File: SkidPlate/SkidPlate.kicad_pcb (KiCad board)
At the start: 2 copper layers, 152.1 x 80.1 mm, 164 parts, among them J2 USB4145-03-0170-C, J3 JST_BM04B-GHS-TBT, J4 JST_2P_LIMITSW, J5 Conn_02x09_Counter_Clockwise, Q2 IRFR3410TRPBF_alternate, Q3 FGH50T65SQD-F155, Q7 FGH50T65SQD-F155, T1 DA2034, U1 RPI2040, U10 SW_TS-1187A-B-A-B, U11 AMP_MCP6231UT_alternate, U2 BNO055, U2 MCP14A0454-E/SN_alternate, U3 AMS1117-3.3, U3 IC_PMW3360DM-T2QU, U4 LT3750, U6 SN65HVD233, U7 MCP2515-xST, U8 AMP_MCP6231UT_alternate, U9 SW_TS-1187A-B-A-B, Y1 XTAL-12MHZ-YXC, Y2 ABM3-8.000MHZ-D2Y-T(alternate)

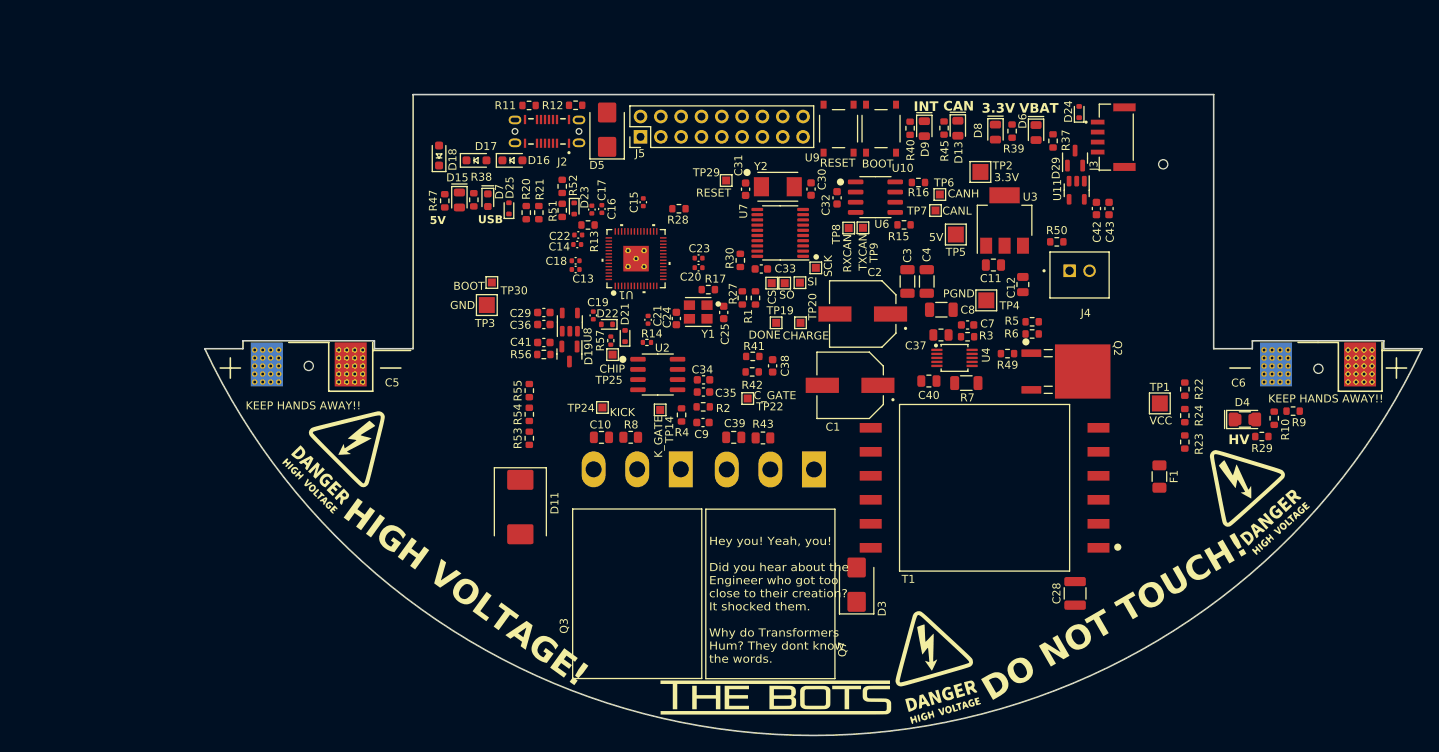
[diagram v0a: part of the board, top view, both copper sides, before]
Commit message: updated skidplate schematic, need to add usb pd
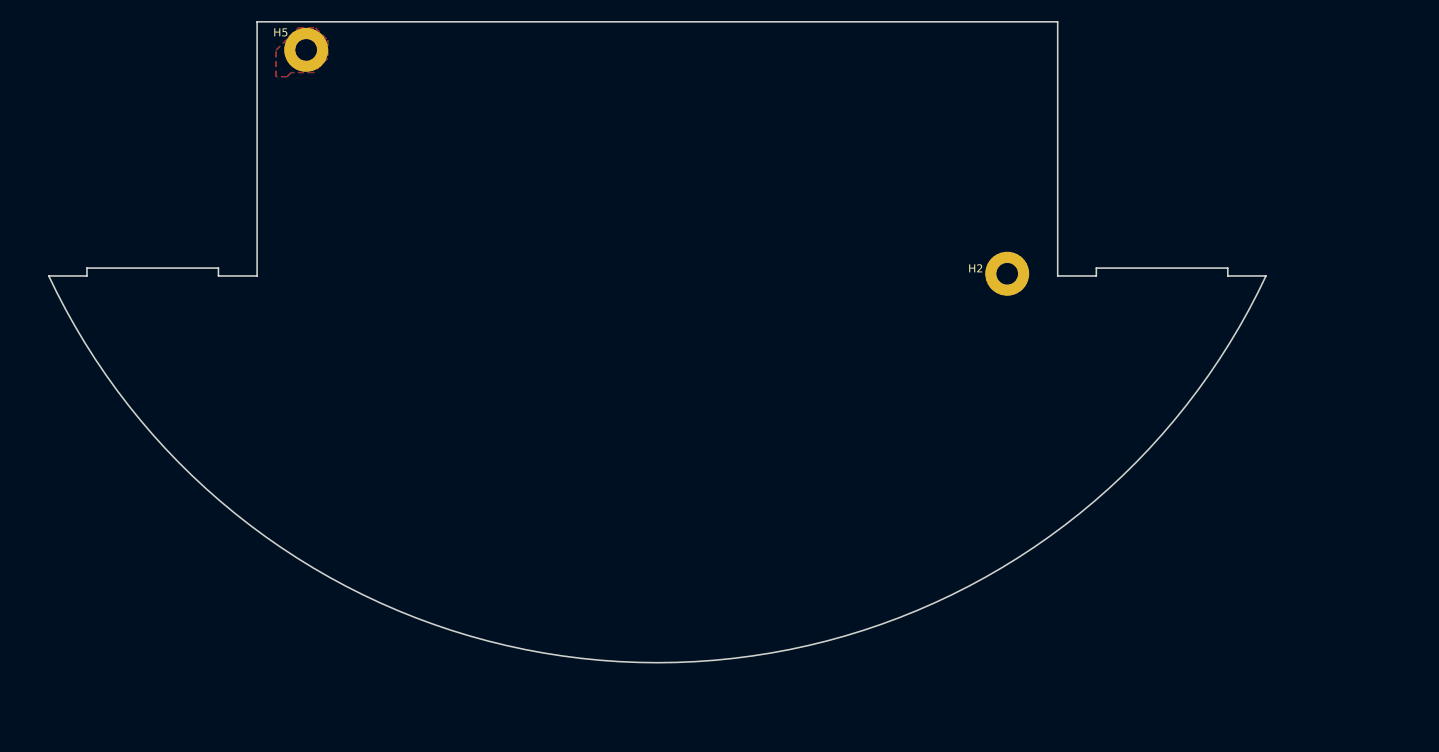
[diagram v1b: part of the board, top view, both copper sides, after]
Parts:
- removed the C1 at (170.6, 106.3)
- removed C10, C39: 1500p, bots:C_0805_2012Metric
- removed C11, C12, C37, C40: 10u, bots:C_0805_2012Metric
- removed C13, C14, C15, C16, C18, C19, C20, C21: 0.1u_0402, bots:C_0402_1005Metric
- removed C17, C22, C23: 1u_0402, bots:C_0402_1005Metric
- removed the C2 at (172.2, 97.4)
- removed C24, C25: 27p, bots:C_0603_1608Metric
- removed C28: 0.1u_600V, bots:C_1210_3225Metric
- removed C29, C41, C43: 0.01u, bots:C_0603_1608Metric
- removed the C3 at (177.8, 93.4)
- removed C30, C31: 22p, bots:C_0603_1608Metric
- removed C32, C33, C34, C38, C9: 0.1u, bots:C_0603_1608Metric
- removed C35, C36, C42: 1u, bots:C_0603_1608Metric
- removed the C4 at (180.2, 93.4)
- removed C5: 1000u, bots:CP_Radial_Horizontal_D25.4mm_H45mm
- removed C6: 1000u, bots:CP_Radial_Horizontal_D25.4mm_H45mm_reversed
- removed C7: 100p, bots:C_0603_1608Metric
- removed C8: 22u_1206, bots:C_1206_3216Metric
- removed D11: MUR860J_alternate, bots:D_SMC
- removed D13, D15, D6, D8, D9: LED, bots:LED_0805_2012Metric
- removed D16, D17, D18: 220mV Schottky, bots:D_SOD-323_HandSoldering
- removed D19, D29: H3V3HT2U, bots:SOT-23
- removed D21, D22, D23, D24, D25: BZT52C3V3T-7, bots:D_SOD-523
- removed D3: MURS160-E3/52T_alternate, bots:D_SMB
- removed D4: LED_red, bots:LED_1206MERGE0805
- removed D5: SMBJ5338B-TP_alternate, bots:D_SMB
- removed D7: LED_blue, bots:LED_0603_1608Metric
- removed F1: 0501010.WR1, bots:Fuse_1206_3216Metric
- removed G*** (x2): SILK_Danger, bots:SILK_Danger
- removed G***: SILK_TheBotsLogo, bots:SILK_TheBotsLogo
- removed G***: LOGO, LOGO
- removed H10, H11, H12: ToolingHoleJLC, bots:ToolingHoleJLC
- removed J2: USB4145-03-0170-C, bots:GCT_USB4145-03-0170-C_REVA2
- removed J3: JST_BM04B-GHS-TBT, bots:JST_BM04B-GHS-TBT
- removed J4: JST_2P_LIMITSW, bots:JST_B2B-XH-A_LF__SN_
- removed J5: Conn_02x09_Counter_Clockwise, bots:PinHeader_2x09_P2.54mm_Vertical
- removed Q2: IRFR3410TRPBF_alternate, bots:DPAK-3_ONS
- removed Q3, Q7: FGH50T65SQD-F155, bots:TO-247-3_Horizontal_TabDown
- removed R1, R10, R27, R29, R50, R9: 100k, bots:R_0603_1608Metric
- removed R11, R12: 5.1k, bots:R_0603_1608Metric
- removed R13: 200R, bots:R_0603_1608Metric
- removed R14, R57: 0R, bots:R_0402_1005Metric
- removed R15, R16, R2, R28, R30, R41: 10k, bots:R_0603_1608Metric
- removed R17, R39: 1k, bots:R_0603_1608Metric
- removed R20, R21: 33R, bots:R_0603_1608Metric
- removed R22: R_200k, bots:R_0603_1608Metric
- removed R23, R24: R_470k, bots:R_0603_1608Metric
- removed R3: 2.4k, bots:R_0603_1608Metric
- removed R37: 47k, bots:R_0603_1608Metric
- removed R38: 820R, bots:R_0603_1608Metric
- removed R4, R42: 75R, bots:R_0603_1608Metric
- removed R40, R45: 510R, bots:R_0603_1608Metric
- removed R43, R8: 2, bots:R_0805_2012Metric
- removed R47: 2k, bots:R_0603_1608Metric
- removed R49: R_0OHM_JUMPER, bots:R_0603_1608Metric
- removed R5: 40.2k, bots:R_0603_1608Metric
- removed R51: 51k, bots:R_0603_1608Metric
- removed R52: 30k, bots:R_0603_1608Metric
- removed R53, R54, R55: 330k, bots:R_0603_1608Metric
- removed R56: 13k, bots:R_0603_1608Metric
- removed R6: 33k, bots:R_0603_1608Metric
- removed R7: 8m, bots:R_1206_3216Metric
- removed T1: DA2034, bots:DA2034-ALD_COC
- removed TP1: VCC, bots:TestPoint_Pad_2.0x2.0mm
- removed TP10: SI, bots:TestPoint_Pad_1.0x1.0mm
- removed TP11: SO, bots:TestPoint_Pad_1.0x1.0mm
- removed TP12: CS, bots:TestPoint_Pad_1.0x1.0mm
- removed TP13: SCK, bots:TestPoint_Pad_1.0x1.0mm
- removed TP14: K_GATE, bots:TestPoint_Pad_1.0x1.0mm
- removed TP19: DONE, bots:TestPoint_Pad_1.0x1.0mm
- removed TP2: 3.3V, bots:TestPoint_Pad_2.0x2.0mm
- removed TP20: CHARGE, bots:TestPoint_Pad_1.0x1.0mm
- removed TP22: C_GATE, bots:TestPoint_Pad_1.0x1.0mm
- removed TP24: KICK, bots:TestPoint_Pad_1.0x1.0mm
- removed TP25: CHIP, bots:TestPoint_Pad_1.0x1.0mm
- removed TP29: RESET, bots:TestPoint_Pad_1.0x1.0mm
- removed TP3: GND, bots:TestPoint_Pad_2.0x2.0mm
- removed TP30: BOOT, bots:TestPoint_Pad_1.0x1.0mm
- removed TP4: PGND, bots:TestPoint_Pad_2.0x2.0mm
- removed TP5: 5V, bots:TestPoint_Pad_2.0x2.0mm
- removed TP6: CANH, bots:TestPoint_Pad_1.0x1.0mm
- removed TP7: CANL, bots:TestPoint_Pad_1.0x1.0mm
- removed TP8: RXCAN, bots:TestPoint_Pad_1.0x1.0mm
- removed TP9: TXCAN, bots:TestPoint_Pad_1.0x1.0mm
- removed the U1 at (143.9, 90.5)
- removed U10, U9: SW_TS-1187A-B-A-B, bots:SW_TS-1187A-B-A-B
- removed U11, U8: AMP_MCP6231UT_alternate, bots:SOT-23-5
- removed the U2 at (146.6, 105.0)
- removed the U3 at (189.9, 85.7)
- removed the U4 at (183.7, 102.9)
- removed U6: SN65HVD233, bots:SOIC-8_3.9x4.9mm_P1.27mm
- removed U7: MCP2515-xST, bots:TSSOP-20_4.4x6.5mm_P0.65mm
- removed Y1: XTAL-12MHZ-YXC, bots:SMD3225-4P
- removed Y2: ABM3-8.000MHZ-D2Y-T(alternate), bots:ABM3
- added H2: PGND, bots:MountingHole_2.7mm_M2.5_DIN965_Pad, F.Cu at (190.3, 92.4)
- added H5: 5V, bots:MountingHole_2.7mm_M2.5_DIN965_Pad, F.Cu at (102.6, 64.4)
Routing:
- added copper zone on F.Cu, net /PowerPillars/5V_IN
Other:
- board text removed: "3.3V"
- board text removed: "5V"
- board text removed: "BOOT"
- board text removed: "CAN"
- board text removed: "DO NOT TOUCH!"
- board text removed: "HIGH VOLTAGE!"
- board text removed: "HV"
- board text removed: "Hey you! Yeah, you! Did you hear about the Engineer who got too close to their creation? It shocked them. Why do Transformers Hum? They dont know the words."
- board text removed: "INT"
- board text removed: "KEEP HANDS AWAY!!"
- board text removed: "RESET"
- board text removed: "USB"
- board text removed: "VBAT"

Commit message: midplate additions WIP
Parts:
- removed C1: 100n, bots:C_0603_1608Metric
- removed C2: 100nF, Capacitor_SMD:C_1206_3216Metric
- removed the H2 at (190.3, 92.4)
- removed the H2 at (-17.7, 86.0)
- removed U3: IC_PMW3360DM-T2QU, bots:IC_PMW3360DM-T2QU 16Pin
- removed U4: ~, Package_TO_SOT_SMD:SOT-223
- added H2: PGND, bots:MountingHole_2.7mm_M2.5_DIN965_Pad, F.Cu at (195.4, 120.4)
- added H3: CANL, bots:MountingHole_2.7mm_M2.5_DIN965_Pad, F.Cu at (195.4, 102.8)
- added H4: CANH, bots:MountingHole_2.7mm_M2.5_DIN965_Pad, F.Cu at (195.4, 92.4)
- added H6: EXTRA, bots:MountingHole_2.7mm_M2.5_DIN965_Pad, F.Cu at (107.7, 124.7)
- added H7: HV, bots:MountingHole_2.7mm_M2.5_DIN965_Pad, F.Cu at (107.7, 133.4)
- added H8: CHICKER, bots:MountingHole_2.7mm_M2.5_DIN965_Pad, F.Cu at (107.7, 142.2)
- added H9: BKBM, bots:MountingHole_2.7mm_M2.5_DIN965_Pad, F.Cu at (107.7, 107.6)
- added J11: XT30UPB-M, bots:AMASS_XT30UPB-M, F.Cu at (41.2, 37.2)
- added J12: XT30UPB-M, bots:AMASS_XT30UPB-M, F.Cu at (41.2, 43.9)
- added J13: XT30UPB-M, bots:AMASS_XT30UPB-M, F.Cu at (41.2, 50.7)
- added J14: XT30UPB-M, bots:AMASS_XT30UPB-M, F.Cu at (41.2, 57.4)
- added J3: JST_BM03B-GHS-TBT, bots:JST_BM03B-GHS-TBT, F.Cu at (56.7, 64.5)
- added J4: JST_BM04B-GHS-TBT, bots:JST_BM04B-GHS-TBT, F.Cu at (57.3, 33.8)
- added J5: JST_BM04B-GHS-TBT, bots:JST_BM04B-GHS-TBT, F.Cu at (57.3, 41.5)
- added J6: JST_BM04B-GHS-TBT, bots:JST_BM04B-GHS-TBT, F.Cu at (57.3, 49.2)
- added J7: JST_BM04B-GHS-TBT, bots:JST_BM04B-GHS-TBT, F.Cu at (57.3, 56.9)
- added R2: 20k, Resistor_SMD:R_0603_1608Metric, F.Cu at (54.3, 68.0)
- added R3: 10k, Resistor_SMD:R_0603_1608Metric, F.Cu at (54.3, 70.5)
- added TP1: SI, bots:pad_0603, F.Cu at (29.4, 70.0)
- added TP11: VCC, bots:TestPoint_Pad_2.0x2.0mm, F.Cu at (29.8, 82.7)
- added TP2: SI, bots:pad_0603, F.Cu at (29.4, 72.4)
- added TP3: SI, bots:pad_0603, F.Cu at (29.4, 74.7)
- added TP4: SI, bots:pad_0603, F.Cu at (29.4, 77.1)
- added TP5: SI, bots:pad_0603, F.Cu at (29.4, 79.5)
- C3: value 10uF -> 10u; footprint Capacitor_SMD:C_1206_3216Metric -> bots:C_0805_2012Metric
- C4: value 10uF -> 22u; footprint bots:CAP_25SVPF100M -> bots:C_0603_1608Metric
- H1: value 5V -> VCC
- U1: value ~ -> AMS1117-3.3; footprint bots:RV1106_PICO_MAX -> bots:SOT-223-3_TabPin2
- U2: value BNO055 -> LSM6DSOX; footprint bots:LGA28R50P4X10_380X520X100 -> bots:PQFN50P300X250X86-14N
- moved H1 222.2 mm to (195.4, 142.2)
- moved U1 69.6 mm to (37.3, 102.4)
- moved U2 54.0 mm to (46.1, 96.8)
- moved C3 49.2 mm to (30.9, 104.8), turned to 180 degrees
- moved C4 44.8 mm to (31.9, 101.2), turned to 90 degrees
- moved H5 28.5 mm to (107.7, 92.4)
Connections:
- H1 pad 1: +5V -> VCC
- H5 pad 1: /PowerPillars/5V_IN -> +5V
- U1 pad 1: unconnected-(U1-GPIO1_B3_d-Pad1) -> GND
- U1 pad 2: unconnected-(U1-GPIO1_B3_u-Pad2) -> +3V3
- U1 pad 3: GND -> +5V
- U2 pad 1: (no net) -> unconnected-(U2-SDO/SA0-Pad1)
- U2 pad 10: /GNDIO -> unconnected-(U2-OCS_AUX-Pad10)
- U2 pad 11: IMU_RST -> unconnected-(U2-SDO_AUX-Pad11)
- U2 pad 12: (no net) -> unconnected-(U2-CS-Pad12)
- U2 pad 13: (no net) -> IMU_SCL
- U2 pad 14: IMU_INT_OUT -> IMU_SDA
- U2 pad 3: +3V3 -> GND
- U2 pad 4: IMU_BOOT_LOAD -> unconnected-(U2-INT1-Pad4)
- U2 pad 5: IMU_PROTOCOL_SELECT_PIN_1 -> unconnected-(U2-VDDIO-Pad5)
- U2 pad 6: IMU_PROTOCOL_SELECT_PIN_0 -> GND
- U2 pad 7: (no net) -> GND
- U2 pad 8: (no net) -> +3V3
- U2 pad 9: Net-(U2-CAP) -> unconnected-(U2-INT2-Pad9)
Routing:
- removed copper zone on F.Cu, net /PowerPillars/5V_IN
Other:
- board size 152.1 x 80.1 mm -> 100.8 x 56.1 mm
